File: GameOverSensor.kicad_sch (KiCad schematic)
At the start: 35 parts

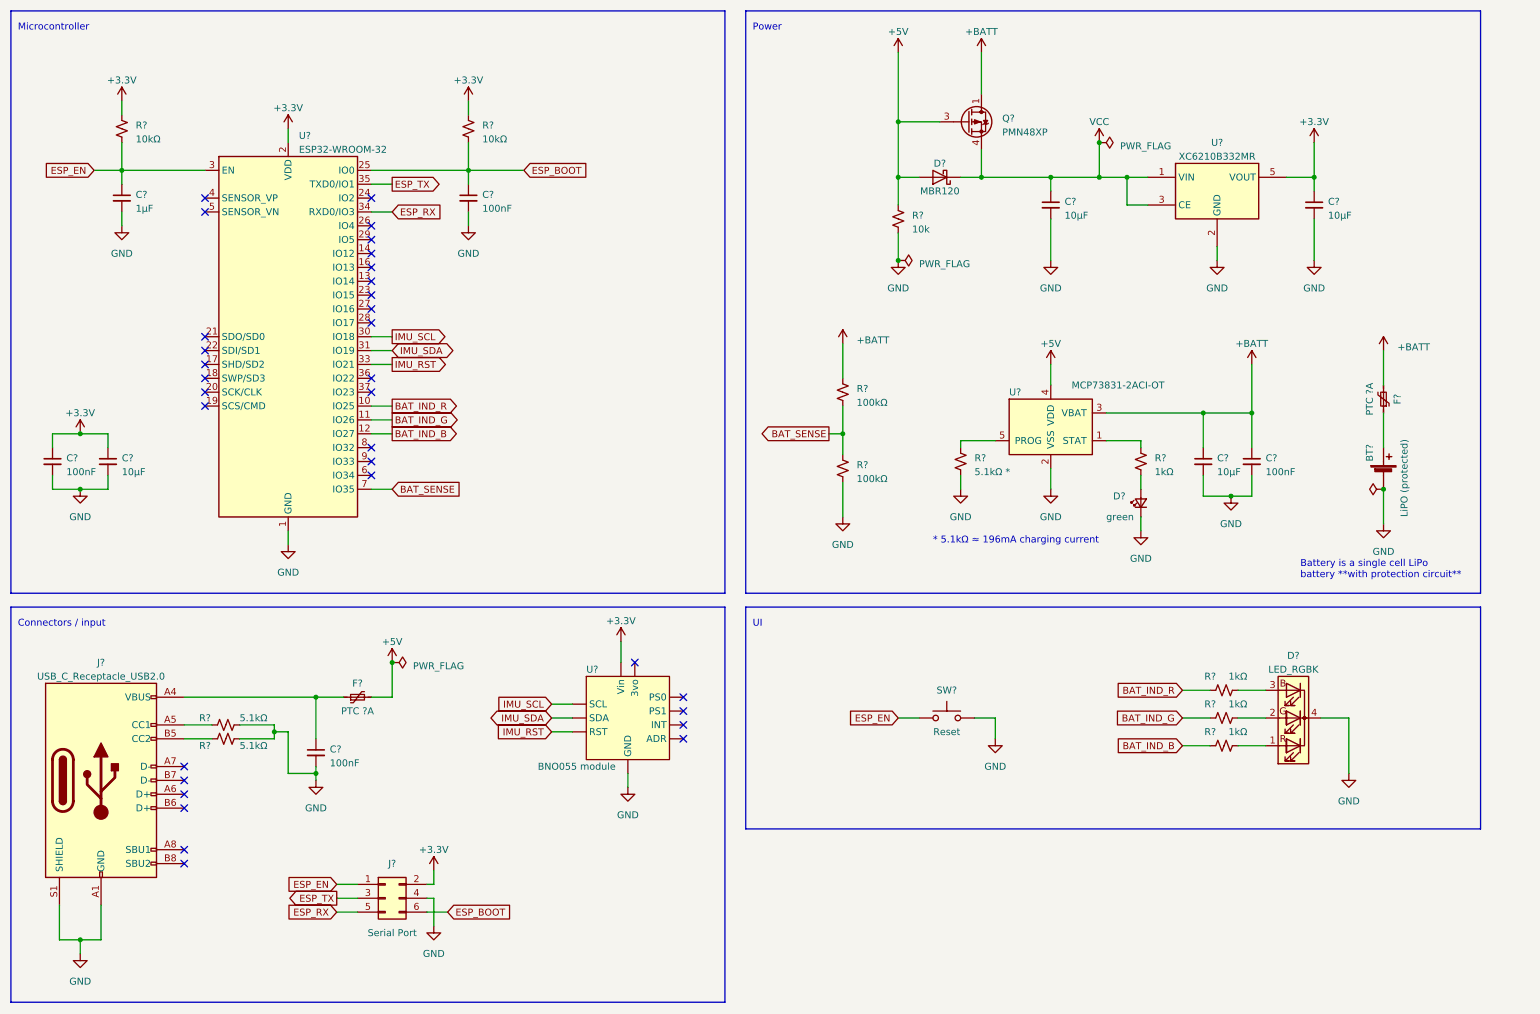
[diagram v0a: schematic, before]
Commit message: Adds circuit to select device ID onboard
We use a 4021 parallel to serial shift register to read the 8 bits of
the ID selected on DIP switches with only 3 pins on the microcontroller.

This comes at some cost in terms of BOM and PCB space, but we're already
running short on pins on the µC.
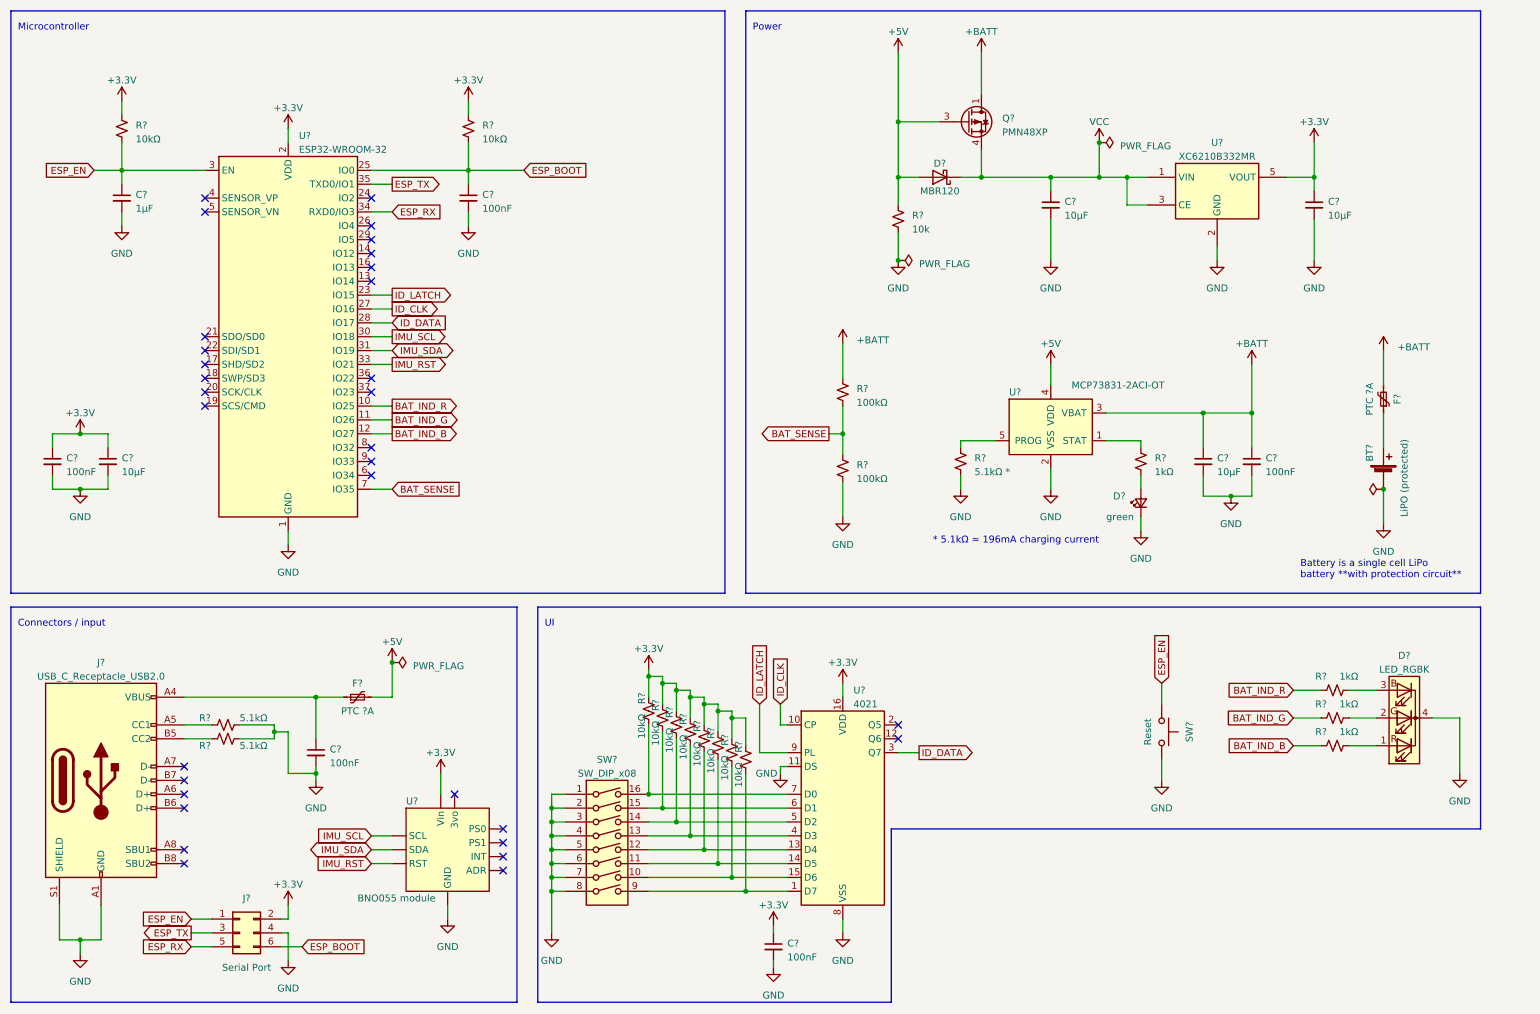
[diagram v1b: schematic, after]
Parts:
- added C?: 100nF, symbol Device:C_Small
- added R? (x8): 10kΩ, symbol Device:R_Small_US
- added SW?: SW_DIP_x08, symbol Switch:SW_DIP_x08
- added U?: 4021, symbol 4xxx:4021
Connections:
- net +3V3: now also C?.1, R?.1, R?.1, R?.1, R?.1, R?.1, R?.1, R?.1, R?.1, U?.16 (VDD)
- net GND: now also C?.2, SW?.1, SW?.2, SW?.3, SW?.4, SW?.5, SW?.6, SW?.7, SW?.8, U?.11 (DS), U?.8 (VSS)
- net ID_LATCH: now reaches U?.23 (IO15)
- net ID_LATCH: now also U?.9 (PL)
- net ID_CLK: now reaches U?.27 (IO16)
- net ID_CLK: now also U?.10 (CP)
- net ID_DATA: now reaches U?.28 (IO17)
- net ID_DATA: now also U?.3 (Q7)
- new net: R?.2, SW?.14, U?.5 (D2)
- new net: R?.2, SW?.12, U?.13 (D4)
- new net: R?.2, SW?.9, U?.1 (D7)
- new net: R?.2, SW?.11, U?.14 (D5)
- new net: R?.2, SW?.10, U?.15 (D6)
- new net: R?.2, SW?.13, U?.4 (D3)
- new net: R?.2, SW?.15, U?.6 (D1)
- new net: R?.2, SW?.16, U?.7 (D0)
- no-connect marks 33 -> 32
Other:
- moved on the sheet: D?, J?, R?, SW?, U?

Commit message: Pulls DIP switches down instead of up
We want the value to be 0 when the switch is open, 1 when it's closed.
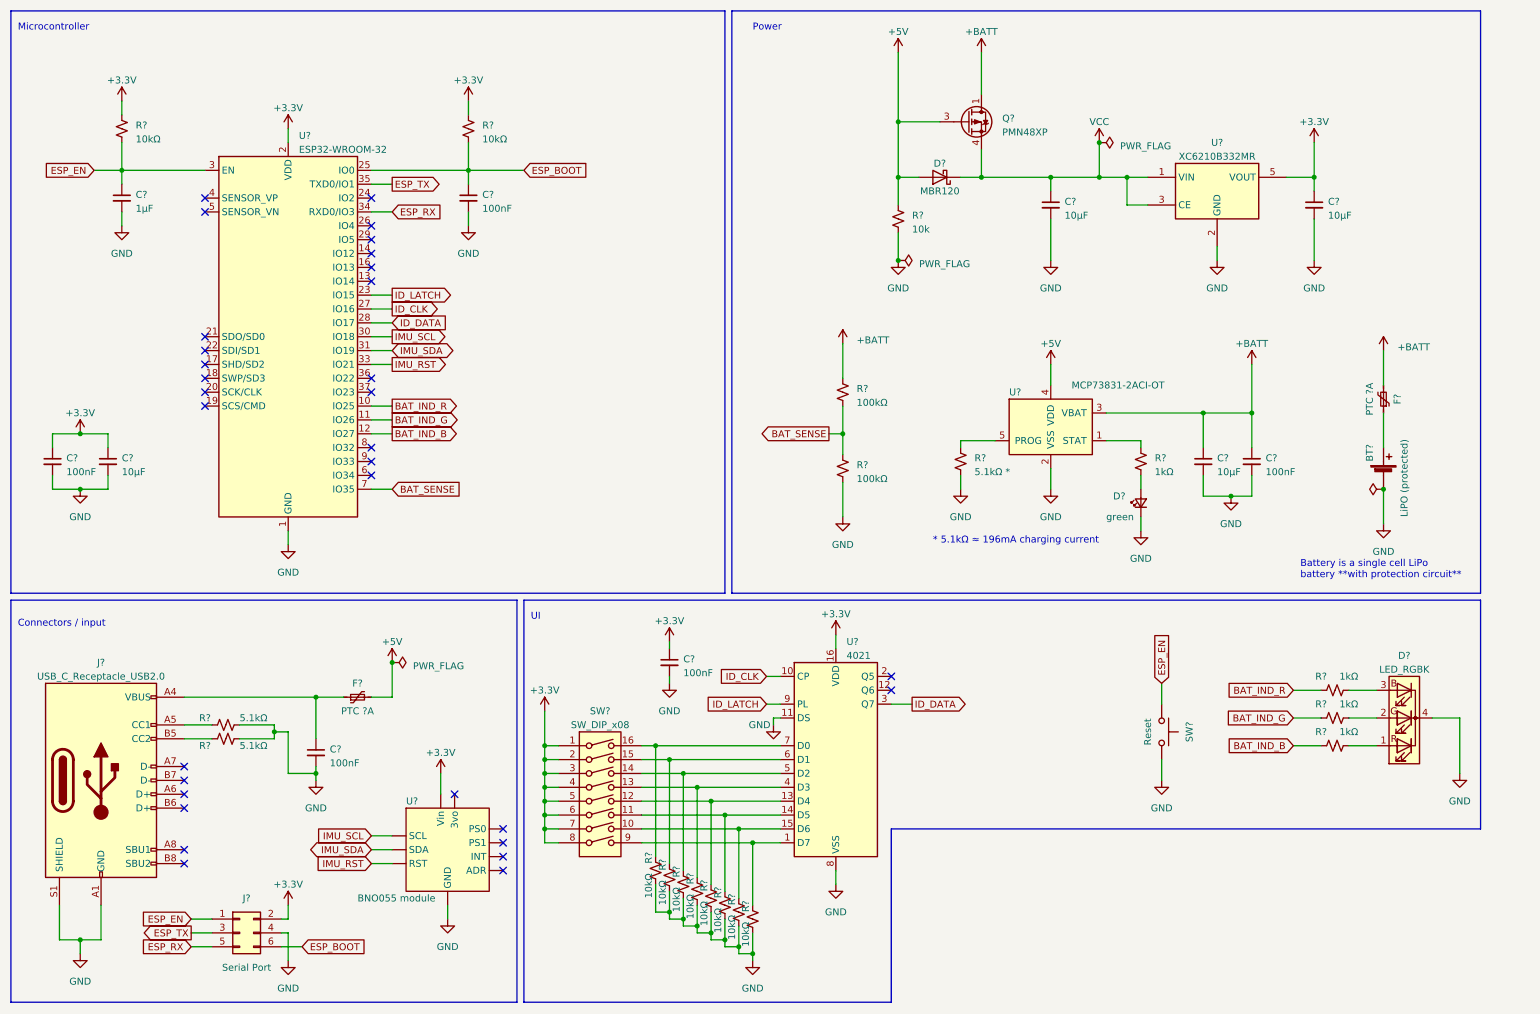
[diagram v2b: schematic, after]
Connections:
- net +3V3: now also SW?.1, SW?.2, SW?.3, SW?.4, SW?.5, SW?.6, SW?.7, SW?.8; no longer R?.1, R?.1, R?.1, R?.1, R?.1, R?.1, R?.1, R?.1
- net GND: now also R?.2, R?.2, R?.2, R?.2, R?.2, R?.2, R?.2, R?.2; no longer SW?.1, SW?.2, SW?.3, SW?.4, SW?.5, SW?.6, SW?.7, SW?.8
- net at SW?.14, U?.5 (D2): now also R?.1; no longer R?.2
- net at SW?.12, U?.13 (D4): now also R?.1; no longer R?.2
- net at SW?.9, U?.1 (D7): now also R?.1; no longer R?.2
- net at SW?.11, U?.14 (D5): now also R?.1; no longer R?.2
- net at SW?.10, U?.15 (D6): now also R?.1; no longer R?.2
- net at SW?.13, U?.4 (D3): now also R?.1; no longer R?.2
- net at SW?.15, U?.6 (D1): now also R?.1; no longer R?.2
- net at SW?.16, U?.7 (D0): now also R?.1; no longer R?.2
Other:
- moved on the sheet: C?, R?, SW?, U?

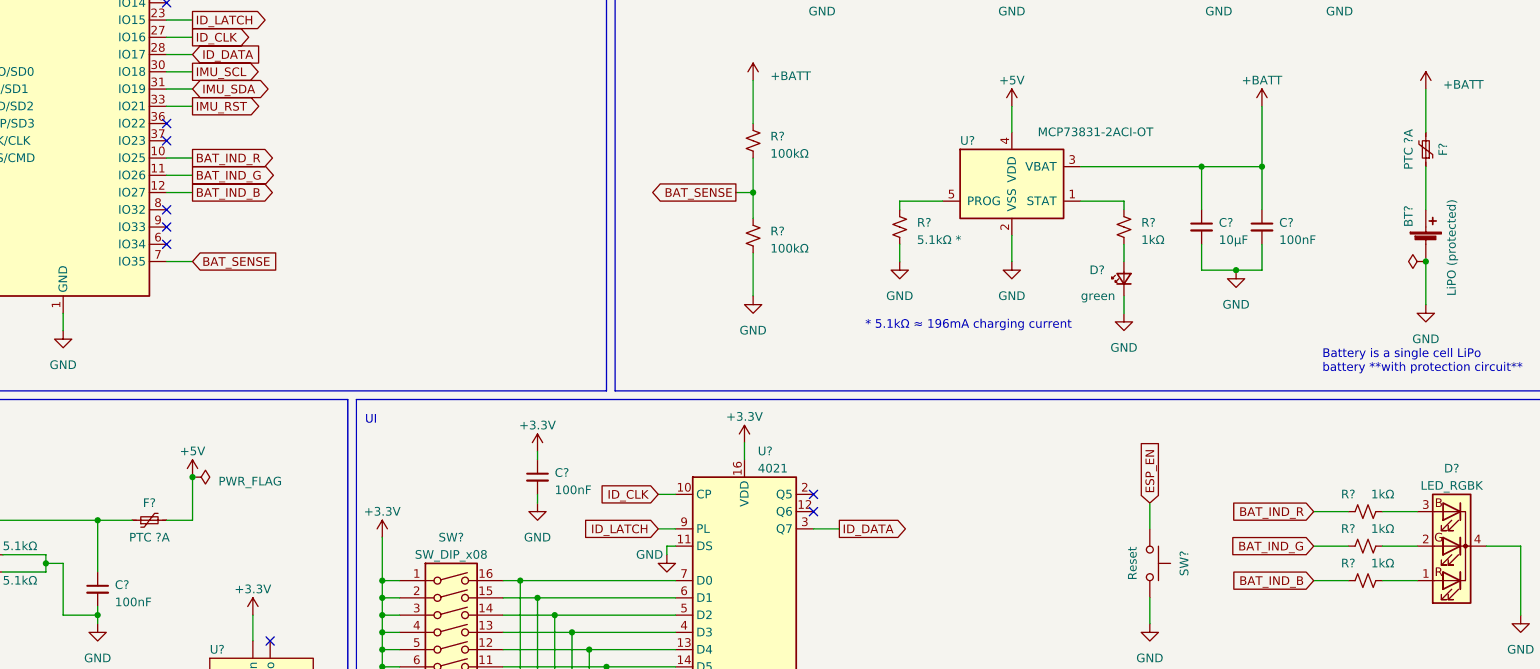
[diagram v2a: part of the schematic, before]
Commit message: Defines PTC fuses to be 1A
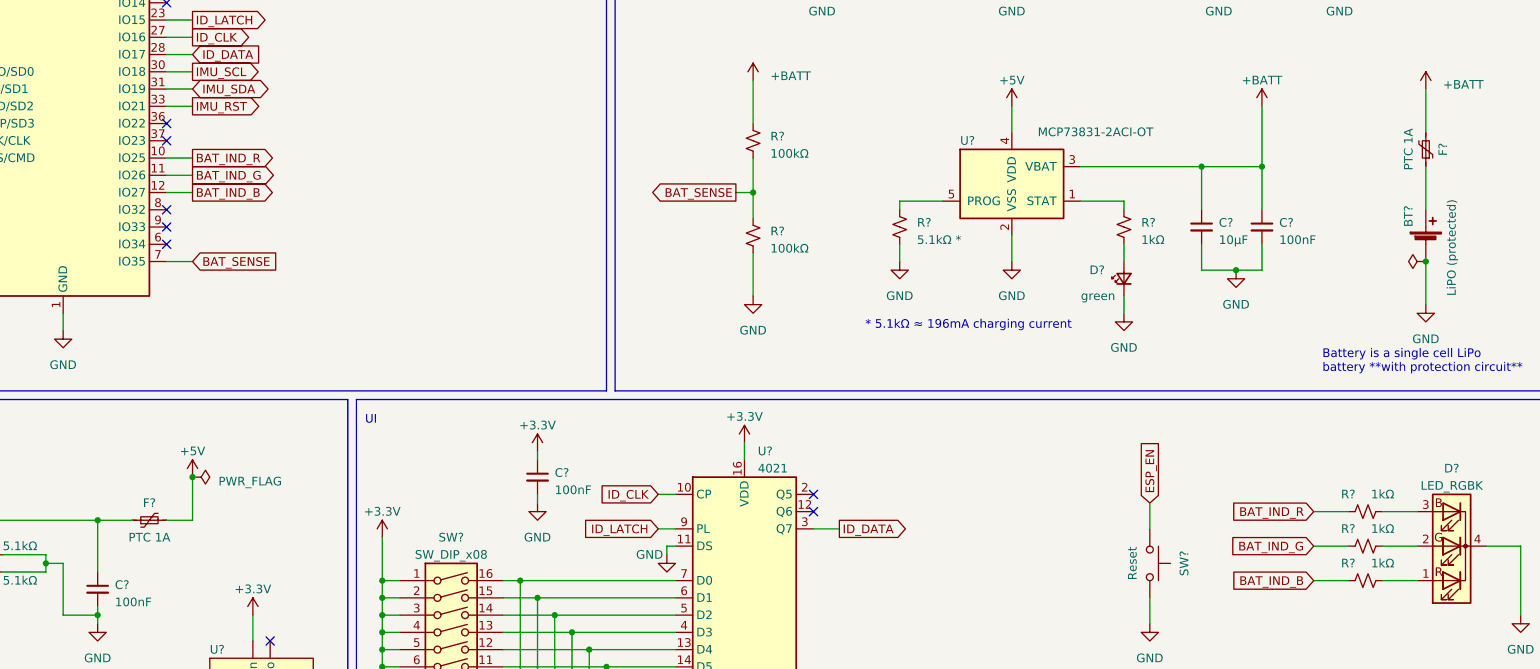
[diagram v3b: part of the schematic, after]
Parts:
- F? (x2): value PTC ?A -> PTC 1A
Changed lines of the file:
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@@
       (effects (font (size 1.27 1.27)))
     )
-    (property "Value" "PTC ?A" (id 1) (at 262.89 85.09 90)
+    (property "Value" "PTC 1A" (id 1) (at 262.89 85.09 90)
       (effects (font (size 1.27 1.27)))
     )
@@
       (effects (font (size 1.27 1.27)))
     )
-    (property "Value" "PTC ?A" (id 1) (at 77.47 142.24 90)
+    (property "Value" "PTC 1A" (id 1) (at 77.47 142.24 90)
       (effects (font (size 1.27 1.27)))
     )
@@
     )
     (path "/30224ecb-a730-47e1-96df-96b1758a1a2f"
-      (reference "F?") (unit 1) (value "PTC ?A") (footprint "")
+      (reference "F?") (unit 1) (value "PTC 1A") (footprint "")
     )
     (path "/cc111127-f001-4494-a46a-df9cfd9d4666"
-      (reference "F?") (unit 1) (value "PTC ?A") (footprint "")
+      (reference "F?") (unit 1) (value "PTC 1A") (footprint "")
     )
     (path "/60060b39-57f0-4f2c-a062-c391396cf2bf"
